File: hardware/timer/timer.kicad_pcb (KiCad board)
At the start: 2 copper layers, 100 x 100 mm, 22 parts, among them J1 RJ45_Shielded, J2 Conn_01x03_Female, U1 WAVGAT_CAN, U2 HT16K33

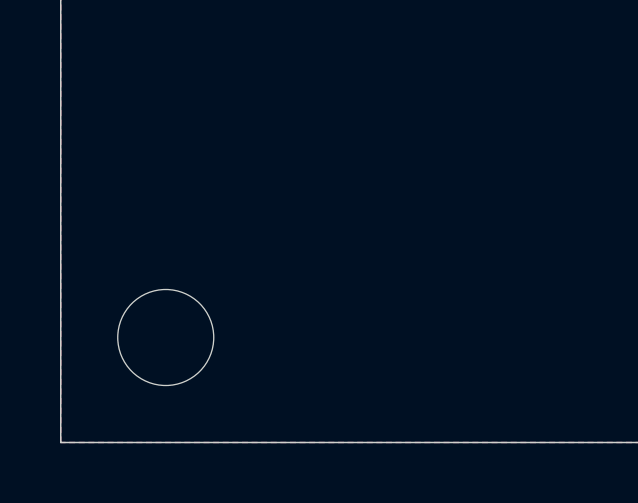
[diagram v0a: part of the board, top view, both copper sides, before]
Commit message: Timer PCB: fix mounting hole location
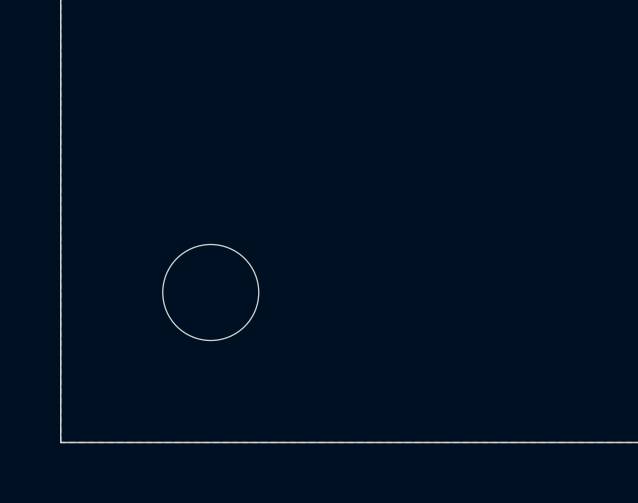
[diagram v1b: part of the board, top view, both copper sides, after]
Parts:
- moved REF** 2.12 mm to (55.0, 145.0)
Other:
- board text added: "BGame Timer v1.0 PurkkaKoodari 2020"

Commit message: Timer PCB: fix kicad router brain fart
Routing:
- net MODULE_ENABLE: track 159.1 -> 127.6 mm
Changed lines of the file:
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@@
-(kicad_pcb (version 20171130) (host pcbnew 5.1.6+dfsg1-1)
+(kicad_pcb (version 20171130) (host pcbnew "(5.1.5)-3")
   (general
     (thickness 1.6)
     (drawings 5)
-    (tracks 260)
+    (tracks 256)
     (zones 0)
     (modules 22)
@@
   )
   (setup
-    (last_trace_width 0.25)
+    (last_trace_width 0.35)
     (user_trace_width 0.25)
     (user_trace_width 0.35)
@@
   (segment (start 88.792 97.268) (end 86.546 97.268) (width 0.35) (layer B.Cu) (net 19))
   (segment (start 69.234 67.654) (end 71.08 69.5) (width 0.35) (layer B.Cu) (net 21))
-  (segment (start 128.935999 79.504999) (end 143.564999 79.504999) (width 0.35) (layer F.Cu) (net 21))
-  (segment (start 95.142 71.614) (end 115.33403 51.42197) (width 0.35) (layer F.Cu) (net 21))
-  (segment (start 143.564999 79.504999) (end 144.74 80.68) (width 0.35) (layer F.Cu) (net 21))
-  (segment (start 81.934 71.614) (end 95.142 71.614) (width 0.35) (layer F.Cu) (net 21))
-  (segment (start 72.776 67.804) (end 78.124 67.804) (width 0.35) (layer F.Cu) (net 21))
-  (segment (start 78.124 67.804) (end 81.934 71.614) (width 0.35) (layer F.Cu) (net 21))
-  (segment (start 115.33403 51.42197) (end 135.179632 51.42197) (width 0.35) (layer F.Cu) (net 21))
-  (segment (start 71.08 69.5) (end 72.776 67.804) (width 0.35) (layer F.Cu) (net 21))
-  (segment (start 135.179632 51.42197) (end 147.80402 64.046358) (width 0.35) (layer F.Cu) (net 21))
-  (segment (start 147.80402 76.814982) (end 145.304001 79.315001) (width 0.35) (layer F.Cu) (net 21))
-  (segment (start 145.304001 79.315001) (end 128.746001 79.315001) (width 0.35) (layer F.Cu) (net 21))
-  (segment (start 147.80402 64.046358) (end 147.80402 76.814982) (width 0.35) (layer F.Cu) (net 21))
-  (segment (start 128.746001 79.315001) (end 128.935999 79.504999) (width 0.35) (layer F.Cu) (net 21))
   (segment (start 68.966 67.386) (end 69.234 67.654) (width 0.35) (layer B.Cu) (net 21))
   (segment (start 68.966 53.326) (end 68.966 67.386) (width 0.35) (layer B.Cu) (net 21))
+  (segment (start 72.776 67.804) (end 71.08 69.5) (width 0.35) (layer F.Cu) (net 21))
+  (segment (start 78.124 67.804) (end 72.776 67.804) (width 0.35) (layer F.Cu) (net 21))
+  (segment (start 81.934 71.614) (end 78.124 67.804) (width 0.35) (layer F.Cu) (net 21))
+  (segment (start 115.33403 51.42197) (end 95.142 71.614) (width 0.35) (layer F.Cu) (net 21))
+  (segment (start 95.142 71.614) (end 81.934 71.614) (width 0.35) (layer F.Cu) (net 21))
+  (segment (start 144.74 80.68) (end 147.80402 77.61598) (width 0.35) (layer F.Cu) (net 21))
+  (segment (start 147.80402 77.61598) (end 147.80402 64.046358) (width 0.35) (layer F.Cu) (net 21))
+  (segment (start 147.80402 64.046358) (end 135.179632 51.42197) (width 0.35) (layer F.Cu) (net 21))
+  (segment (start 135.179632 51.42197) (end 115.33403 51.42197) (width 0.35) (layer F.Cu) (net 21))
   (segment (start 69.81 72.04) (end 69.81 73.206) (width 0.35) (layer B.Cu) (net 23))
   (segment (start 69.81 73.206) (end 70.25 73.646) (width 0.35) (layer B.Cu) (net 23))
